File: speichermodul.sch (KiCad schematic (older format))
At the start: 64 parts, among them IC1 6116, P1 CONN_3X2, P2 CONN_01X01, P3 CONN_01X01, P4 CONN_01X01, P5 CONN_01X01, P6 CONN_01X01, P7 CONN_01X01, P8 CONN_02X10, P9 CONN_02X10, SW1 SW_PUSH, SW2 SW_PUSH, U1 7400, U2 74LS08, U3 74LS08, U4 74LS14, U5 74LS540, U6 74LS540

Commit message: Pcb layout kabelverlegt
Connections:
- net GND: no longer D10.1 (K), D11.1 (K), D12.1 (K), D13.1 (K), D14.1 (K), D15.1 (K), D16.1 (K), D17.1 (K), D18.1 (K), D3.1 (K), D4.1 (K), D5.1 (K), D6.1 (K), D7.1 (K), D8.1 (K), D9.1 (K)
- net VCC: now also D10.2 (A), D11.2 (A), D12.2 (A), D13.2 (A), D14.2 (A), D15.2 (A), D16.2 (A), D17.2 (A), D18.2 (A), D3.2 (A), D4.2 (A), D5.2 (A), D6.2 (A), D7.2 (A), D8.2 (A), D9.2 (A)
- net at R4.1: now also D10.1 (K); no longer D3.2 (A)
- net at R9.1: now also D9.1 (K); no longer D4.2 (A)
- net at R10.1: now also D8.1 (K); no longer D5.2 (A)
- net at R11.1: now also D7.1 (K); no longer D6.2 (A)
- net at R12.1: now also D6.1 (K); no longer D7.2 (A)
- net at R13.1: now also D5.1 (K); no longer D8.2 (A)
- net at R14.1: now also D4.1 (K); no longer D9.2 (A)
- net at R15.1: now also D3.1 (K); no longer D10.2 (A)
- net at R16.1: now also D18.1 (K); no longer D11.2 (A)
- net at R17.1: now also D17.1 (K); no longer D12.2 (A)
- net at R18.1: now also D16.1 (K); no longer D13.2 (A)
- net at R19.1: now also D15.1 (K); no longer D14.2 (A)
- net at R20.1: now also D14.1 (K); no longer D15.2 (A)
- net at R21.1: now also D13.1 (K); no longer D16.2 (A)
- net at R22.1: now also D12.1 (K); no longer D17.2 (A)
- net at R23.1: now also D11.1 (K); no longer D18.2 (A)
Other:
- moved on the sheet: D10, D11, D12, D13, D14, D15, D16, D17, D18, D3, D4, D5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

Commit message: PCB layout revolutioniert
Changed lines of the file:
@@
 Wire Wire Line
 	5800 1550 5800 1650
+Connection ~ 5800 1650
+Wire Wire Line
+	5800 1650 5800 1850
+Wire Wire Line
+	37600 -12100 37600 -21800
+Wire Wire Line
+	37600 -21800 42950 -21800
+Wire Wire Line
+	42950 -21800 42950 -11850
+Wire Wire Line
+	42950 -11850 54850 -11850
+Wire Wire Line
+	54850 -11850 54850 -1350
+Wire Wire Line
+	54850 -1350 47700 -1350
+Wire Wire Line
+	47700 -1350 47700 20550
+Wire Wire Line
+	47700 20550 41950 20550
+Wire Wire Line
+	41950 20550 41950 12350
+Wire Wire Line
+	41950 12350 38500 12350
+Wire Wire Line
+	38500 12350 38500 20300
+Wire Wire Line
+	38500 20300 32700 20300
+Wire Wire Line
+	32700 20300 32700 -3000
+Wire Wire Line
+	32700 -3000 22850 -3000
+Wire Wire Line
+	22850 -3000 22850 -6100
+Wire Wire Line
+	22850 -6100 18500 -6100
+Wire Wire Line
+	18500 -6100 18500 -8000
+Wire Wire Line
+	18500 -8000 22500 -8000
+Wire Wire Line
+	18500 -8000 18500 -9000
+Wire Wire Line
+	18500 -9000 22500 -9000
+Connection ~ 18500 -8000
+Wire Wire Line
+	14550 -12100 37600 -12100
+Wire Wire Line
+	14550 -12100 14550 -9800
+Wire Wire Line
+	18500 -9000 18500 -9800
+Connection ~ 18500 -9000
+Wire Wire Line
+	18500 -9800 14550 -9800
+Wire Wire Line
+	38600 -18050 39500 -18050
+Wire Wire Line
+	39500 -18050 39500 -17550
+Wire Wire Line
+	39500 -17550 38600 -17550
+Wire Wire Line
+	38600 -17550 38600 -18050
+Wire Wire Line
+	41150 -17500 42450 -17500
+Wire Wire Line
+	42450 -17500 42450 -18050
+Wire Wire Line
+	42450 -18050 41150 -18050
+Wire Wire Line
+	41150 -18050 41150 -17500
+Wire Wire Line
+	39950 -15200 40600 -15200
+Wire Wire Line
+	40600 -15200 40600 -16450
+Wire Wire Line
+	40600 -16450 39950 -16450
+Wire Wire Line
+	39950 -16450 39950 -15200
+Wire Wire Line
+	38400 -13700 38800 -13700
+Wire Wire Line
+	38800 -13700 38800 -13200
+Wire Wire Line
+	38800 -13200 39350 -13200
+Wire Wire Line
+	39350 -13200 39350 -12650
+Wire Wire Line
+	39350 -12650 41600 -12650
+Wire Wire Line
+	41600 -12650 41600 -13100
+Wire Wire Line
+	41600 -13100 42150 -13100
+Wire Wire Line
+	42150 -13100 42150 -13700
+Wire Wire Line
+	42150 -13700 42600 -13700
+Wire Wire Line
+	42600 -13700 42600 -14300
+Wire Wire Line
+	42600 -14300 41850 -14300
+Wire Wire Line
+	41850 -14300 41850 -13600
+Wire Wire Line
+	41850 -13600 41500 -13600
+Wire Wire Line
+	41500 -13600 41500 -13150
+Wire Wire Line
+	41500 -13150 39650 -13150
+Wire Wire Line
+	39650 -13150 39650 -13650
+Wire Wire Line
+	39650 -13650 39200 -13650
+Wire Wire Line
+	39200 -13650 39200 -14050
+Wire Wire Line
+	39200 -14050 38400 -14050
+Wire Wire Line
+	38400 -14050 38400 -13700
 Wire Bus Line
 	9550 3350 9550 3550
@@
 Wire Bus Line
 	10950 2750 10950 4850
-Connection ~ 5800 1650
-Wire Wire Line
-	5800 1650 5800 1850
 $EndSCHEMATC

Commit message: minimal änderungen
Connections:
- wire segments 262 -> 274
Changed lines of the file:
@@
 Wire Wire Line
 	38400 -14050 38400 -13700
+Wire Wire Line
+	55750 -26500 55750 -14450
+Wire Wire Line
+	55750 -14450 66900 -14450
+Wire Wire Line
+	71650 -25450 71650 -18950
+Wire Wire Line
+	71650 -18950 58050 -18950
+Wire Wire Line
+	66750 -25350 57150 -25350
+Wire Wire Line
+	57150 -25350 57150 -15850
+Wire Wire Line
+	57150 -15850 72550 -15850
+Wire Wire Line
+	60750 -21750 69950 -21750
+Wire Wire Line
+	69950 -21750 69950 -27500
+Wire Wire Line
+	69950 -27500 75100 -27500
+Wire Wire Line
+	75100 -27500 75100 -15100
+Wire Wire Line
+	75100 -15100 57050 -15100
 Wire Bus Line
 	9550 3350 9550 3550

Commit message: Nix
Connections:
- wire segments 274 -> 275
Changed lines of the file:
@@
 U 1 1 57D5C572
 P 9850 5250
-F 0 "P9" H 9850 5800 50  0000 C CNN
+F 0 "P9" H 9850 4650 50  0000 C CNN
 F 1 "CONN_02X10" V 9850 5250 50  0000 C CNN
 F 2 "Connect:IDC_Header_Straight_20pins" H 9850 4050 60  0001 C CNN
 F 3 "" H 9850 4050 60  0000 C CNN
 	1    9850 5250
-	-1   0    0    -1
+	-1   0    0    1
 $EndComp
 $Comp
@@
 F 3 "" H 9850 5800 60  0000 C CNN
 	1    9850 5800
-	-1   0    0    -1
+	1    0    0    -1
 $EndComp
-Text Notes 9650 4650 0    60   ~ 0
+Text Notes 10450 4800 0    60   ~ 0
 Datenbus
 Text Notes 10250 700  0    60   ~ 0
@@
 Wire Wire Line
 	10200 1850 10200 1750
-Wire Wire Line
-	10100 4800 10100 4650
-Wire Wire Line
-	10100 4650 9600 4650
-Wire Wire Line
-	10100 5800 10100 5700
 Wire Bus Line
 	10950 4850 10200 4850
@@
 	1300 4150 1300 4250
 Wire Wire Line
-	9600 5800 9850 5800
-Connection ~ 9850 5800
-Wire Wire Line
-	9850 5800 10100 5800
-Wire Wire Line
-	9600 4650 9600 4800
-Connection ~ 9600 5700
-Wire Wire Line
-	9600 5700 9600 5800
+	9600 4700 9850 4700
+Connection ~ 9850 4700
+Wire Wire Line
+	9850 4700 10100 4700
 Connection ~ 9600 4800
 Wire Wire Line
-	9600 4800 9600 4900
+	9600 4800 9600 4700
+Wire Wire Line
+	9600 5700 9600 5600
+Connection ~ 9600 5600
+Wire Wire Line
+	9600 5600 9600 5500
+Connection ~ 9600 5500
+Wire Wire Line
+	9600 5500 9600 5400
+Connection ~ 9600 5400
+Wire Wire Line
+	9600 5400 9600 5300
+Connection ~ 9600 5300
+Wire Wire Line
+	9600 5300 9600 5200
+Connection ~ 9600 5200
+Wire Wire Line
+	9600 5200 9600 5100
+Connection ~ 9600 5100
+Wire Wire Line
+	9600 5100 9600 5000
+Connection ~ 9600 5000
+Wire Wire Line
+	9600 5000 9600 4900
 Connection ~ 9600 4900
 Wire Wire Line
-	9600 4900 9600 5000
-Connection ~ 9600 5000
-Wire Wire Line
-	9600 5000 9600 5100
-Connection ~ 9600 5100
-Wire Wire Line
-	9600 5100 9600 5200
-Connection ~ 9600 5200
-Wire Wire Line
-	9600 5200 9600 5300
-Connection ~ 9600 5300
-Wire Wire Line
-	9600 5300 9600 5400
-Connection ~ 9600 5400
-Wire Wire Line
-	9600 5400 9600 5500
-Connection ~ 9600 5500
-Wire Wire Line
-	9600 5500 9600 5600
-Connection ~ 9600 5600
-Wire Wire Line
-	9600 5600 9600 5700
+	9600 4900 9600 4800
 Wire Wire Line
 	1300 2850 1300 2950
@@
 Wire Wire Line
 	75100 -15100 57050 -15100
+Wire Wire Line
+	10100 5800 10100 5700
+Wire Wire Line
+	10100 4700 10100 4800
+Wire Wire Line
+	10100 5800 9850 5800
+Wire Wire Line
+	9600 5800 9600 5700
 Wire Bus Line
 	9550 3350 9550 3550
@@
 	8100 1050 8100 1750
 Wire Bus Line
+	10950 2750 10950 4850
+Wire Bus Line
+	10200 4850 10200 6450
+Wire Bus Line
+	9550 2500 9550 3250
+Wire Bus Line
+	10100 850  10100 2500
+Wire Bus Line
+	9350 1200 9350 1750
+Wire Bus Line
 	7300 5750 7300 6450
-Wire Bus Line
-	9350 1200 9350 1750
-Wire Bus Line
-	10100 850  10100 2500
-Wire Bus Line
-	9550 2500 9550 3250
-Wire Bus Line
-	10200 4850 10200 6450
-Wire Bus Line
-	10950 2750 10950 4850
+Connection ~ 9600 5700
+Connection ~ 9850 5800
+Wire Wire Line
+	9850 5800 9600 5800
 $EndSCHEMATC

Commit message: mit Korrektur der Anordnung begonnen
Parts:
- removed RP3: R_PACK8BUSSED, Housings_SIP:SIP9_Housing_BigPads, symbol speichermodul-rescue:R_PACK8BUSSED-RESCUE-speichermodul
- SW1, SW2: footprint Buttons_Switches_ThroughHole:SW_PUSH_6mm_h5mm -> tg_foodprint:SW_PUSH_LCD_E3_SAxxxx_tg
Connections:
- wire segments 275 -> 280
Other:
- moved on the sheet: RP2
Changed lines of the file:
@@
 F 0 "SW2" H 1150 4960 50  0000 C CNN
 F 1 "SW_PUSH" H 1000 4770 50  0000 C CNN
-F 2 "Buttons_Switches_ThroughHole:SW_PUSH_6mm_h5mm" H 1000 4850 60  0001 C CNN
+F 2 "tg_foodprint:SW_PUSH_LCD_E3_SAxxxx_tg" H 1000 4850 60  0001 C CNN
 F 3 "~" H 1000 4850 60  0000 C CNN
 	1    1000 4850
@@
 F 0 "SW1" H 1150 2760 50  0000 C CNN
 F 1 "SW_PUSH" H 1000 2570 50  0000 C CNN
-F 2 "Buttons_Switches_ThroughHole:SW_PUSH_6mm_h5mm" H 1000 2650 60  0001 C CNN
+F 2 "tg_foodprint:SW_PUSH_LCD_E3_SAxxxx_tg" H 1000 2650 60  0001 C CNN
 F 3 "~" H 1000 2650 60  0000 C CNN
 	1    1000 2650
@@
 L speichermodul-rescue:R_PACK8BUSSED-RESCUE-speichermodul RP2
 U 1 1 57D77728
-P 9050 1250
-F 0 "RP2" H 9050 1550 50  0000 C CNN
-F 1 "R_PACK8BUSSED" H 9050 950 50  0000 C CNN
-F 2 "Housings_SIP:SIP9_Housing_BigPads" H 9050 1300 60  0001 C CNN
-F 3 "~" H 9050 1300 60  0000 C CNN
-	1    9050 1250
+P 9000 1250
+F 0 "RP2" H 9000 1550 50  0000 C CNN
+F 1 "R_PACK8BUSSED" H 9000 950 50  0000 C CNN
+F 2 "Housings_SIP:SIP9_Housing_BigPads" H 9000 1300 60  0001 C CNN
+F 3 "~" H 9000 1300 60  0000 C CNN
+	1    9000 1250
 	-1   0    0    -1
 $EndComp
@@
 Wire Wire Line
 	9350 1050 9350 1000
-$Comp
-L speichermodul-rescue:R_PACK8BUSSED-RESCUE-speichermodul RP3
-U 1 1 57D77ABD
-P 7000 5800
-F 0 "RP3" H 7000 6100 50  0000 C CNN
-F 1 "R_PACK8BUSSED" H 7000 5500 50  0000 C CNN
-F 2 "Housings_SIP:SIP9_Housing_BigPads" H 7000 5850 60  0000 C CNN
-F 3 "~" H 7000 5850 60  0000 C CNN
-	1    7000 5800
-	-1   0    0    -1
-$EndComp
-$Comp
-L speichermodul-rescue:VCC-RESCUE-speichermodul #PWR025
-U 1 1 57D77ACC
-P 7300 5550
-F 0 "#PWR025" H 7300 5400 50  0001 C CNN
-F 1 "VCC" H 7300 5700 50  0000 C CNN
-F 2 "" H 7300 5550 60  0000 C CNN
-F 3 "" H 7300 5550 60  0000 C CNN
-	1    7300 5550
-	1    0    0    -1
-$EndComp
-Wire Wire Line
-	7300 5600 7300 5550
 Wire Bus Line
 	4450 6450 10200 6450
 Entry Wire Line
-	7200 5650 7300 5750
-Entry Wire Line
-	7200 5700 7300 5800
-Entry Wire Line
-	7200 5750 7300 5850
-Entry Wire Line
-	7200 5800 7300 5900
-Entry Wire Line
-	7200 5850 7300 5950
-Entry Wire Line
-	7200 5900 7300 6000
-Entry Wire Line
-	7200 5950 7300 6050
-Entry Wire Line
-	7200 6000 7300 6100
-Wire Wire Line
-	7300 5600 7200 5600
-Text Label 7200 5650 0    60   ~ 0
-D0
-Text Label 7200 5700 0    60   ~ 0
-D1
-Text Label 7200 5750 0    60   ~ 0
-D2
-Text Label 7200 5800 0    60   ~ 0
-D3
-Text Label 7200 5850 0    60   ~ 0
-D4
-Text Label 7200 5900 0    60   ~ 0
-D5
-Text Label 7200 5950 0    60   ~ 0
-D6
-Text Label 7200 6000 0    60   ~ 0
-D7
-Entry Wire Line
 	9250 1100 9350 1200
 Entry Wire Line
@@
 Entry Wire Line
 	9250 1450 9350 1550
-Wire Wire Line
-	9250 1050 9350 1050
 Text Label 9250 1100 0    60   ~ 0
 A0
@@
 Wire Wire Line
 	1300 4150 1300 4250
-Wire Wire Line
-	9600 4700 9850 4700
-Connection ~ 9850 4700
-Wire Wire Line
-	9850 4700 10100 4700
 Connection ~ 9600 4800
 Wire Wire Line
@@
 Wire Wire Line
 	9600 5800 9600 5700
+Connection ~ 9600 5700
+Connection ~ 9850 5800
+Wire Wire Line
+	9850 5800 9600 5800
+Wire Wire Line
+	9600 4700 10100 4700
+Wire Wire Line
+	9200 1050 9350 1050
+Wire Wire Line
+	9250 1100 9200 1100
+Wire Wire Line
+	9200 1150 9250 1150
+Wire Wire Line
+	9250 1200 9200 1200
+Wire Wire Line
+	9200 1250 9250 1250
+Wire Wire Line
+	9250 1300 9200 1300
+Wire Wire Line
+	9200 1350 9250 1350
+Wire Wire Line
+	9250 1400 9200 1400
+Wire Wire Line
+	9200 1450 9250 1450
 Wire Bus Line
 	9550 3350 9550 3550
@@
 Wire Bus Line
 	9350 1200 9350 1750
-Wire Bus Line
-	7300 5750 7300 6450
-Connection ~ 9600 5700
-Connection ~ 9850 5800
-Wire Wire Line
-	9850 5800 9600 5800
 $EndSCHEMATC

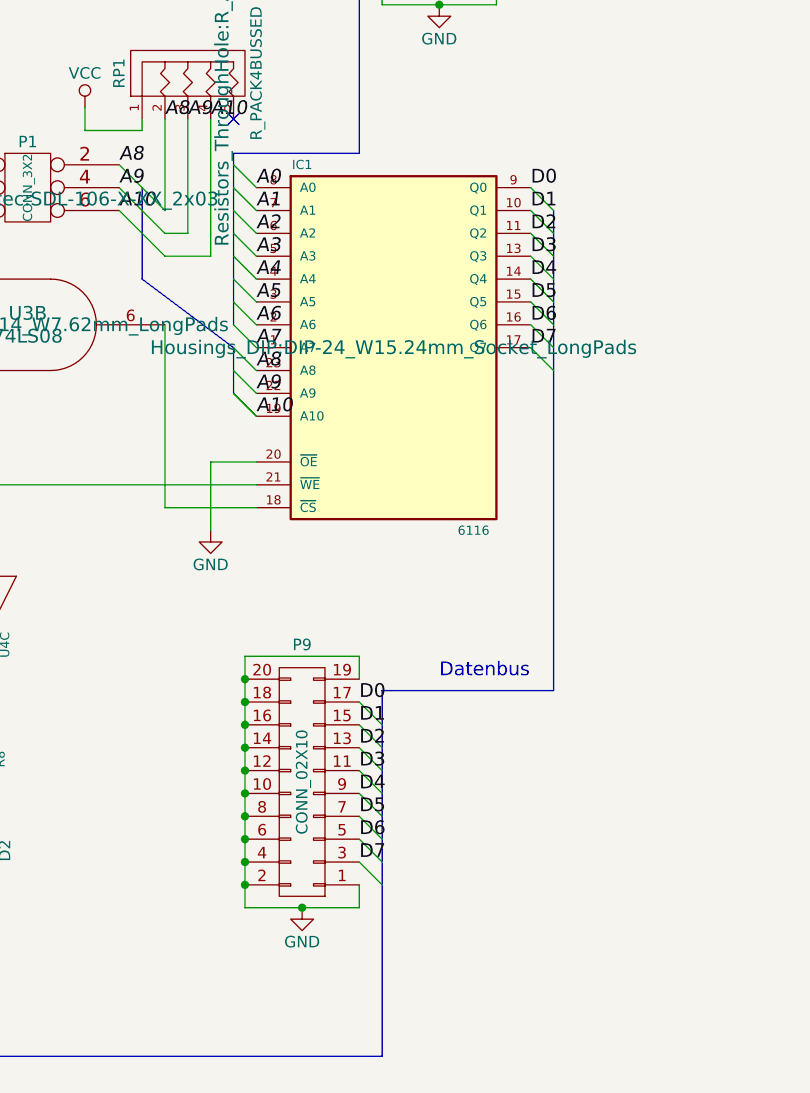
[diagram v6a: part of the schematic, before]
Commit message: busses new arranged
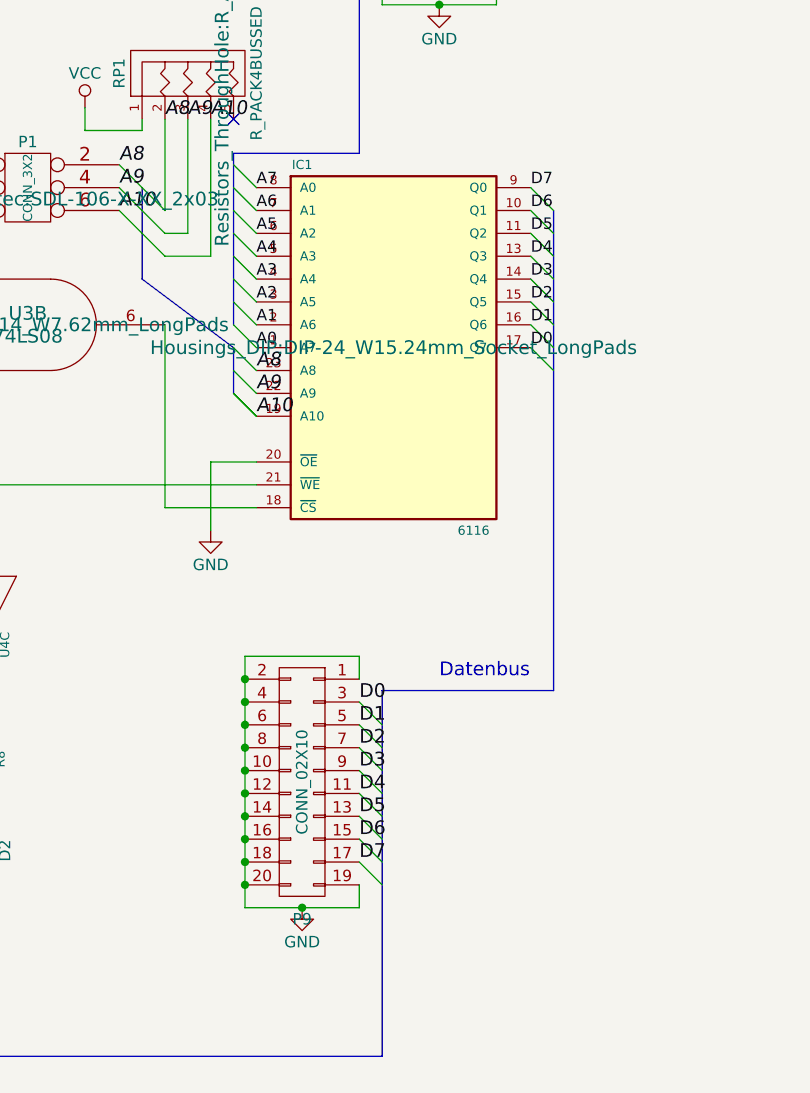
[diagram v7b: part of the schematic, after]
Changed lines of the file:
@@
 F 3 "" H 9850 4050 60  0000 C CNN
 	1    9850 5250
-	-1   0    0    1
+	-1   0    0    -1
 $EndComp
 $Comp
@@
 Entry Wire Line
 	10850 2650 10950 2750
-Text Label 10850 2650 0    60   ~ 0
-D0
-Text Label 10850 2750 0    60   ~ 0
-D1
-Text Label 10850 2850 0    60   ~ 0
-D2
-Text Label 10850 2950 0    60   ~ 0
-D3
-Text Label 10850 3050 0    60   ~ 0
-D4
-Text Label 10850 3150 0    60   ~ 0
-D5
-Text Label 10850 3250 0    60   ~ 0
-D6
-Text Label 10850 3350 0    60   ~ 0
-D7
 Entry Wire Line
 	10850 2750 10950 2850
@@
 Text Label 10200 1650 0    60   Italic 0
 A7
-Text Label 9650 2650 0    60   Italic 0
-A0
-Text Label 9650 2750 0    60   Italic 0
-A1
-Text Label 9650 2850 0    60   Italic 0
-A2
-Text Label 9650 2950 0    60   Italic 0
-A3
-Text Label 9650 3050 0    60   Italic 0
-A4
-Text Label 9650 3150 0    60   Italic 0
-A5
-Text Label 9650 3250 0    60   Italic 0
-A6
-Text Label 9650 3350 0    60   Italic 0
-A7
-Entry Wire Line
-	9550 2550 9650 2650
-Entry Wire Line
-	9550 2650 9650 2750
-Entry Wire Line
-	9550 2750 9650 2850
-Entry Wire Line
-	9550 2850 9650 2950
-Entry Wire Line
-	9550 2950 9650 3050
-Entry Wire Line
-	9550 3050 9650 3150
-Entry Wire Line
-	9550 3150 9650 3250
-Entry Wire Line
-	9550 3250 9650 3350
 Connection ~ 1150 4150
 Wire Wire Line
@@
 Wire Wire Line
 	1300 4150 1300 4250
-Connection ~ 9600 4800
-Wire Wire Line
-	9600 4800 9600 4700
-Wire Wire Line
-	9600 5700 9600 5600
-Connection ~ 9600 5600
-Wire Wire Line
-	9600 5600 9600 5500
-Connection ~ 9600 5500
-Wire Wire Line
-	9600 5500 9600 5400
-Connection ~ 9600 5400
-Wire Wire Line
-	9600 5400 9600 5300
-Connection ~ 9600 5300
-Wire Wire Line
-	9600 5300 9600 5200
-Connection ~ 9600 5200
-Wire Wire Line
-	9600 5200 9600 5100
-Connection ~ 9600 5100
-Wire Wire Line
-	9600 5100 9600 5000
-Connection ~ 9600 5000
-Wire Wire Line
-	9600 5000 9600 4900
-Connection ~ 9600 4900
-Wire Wire Line
-	9600 4900 9600 4800
 Wire Wire Line
 	1300 2850 1300 2950
@@
 Wire Wire Line
 	10100 5800 9850 5800
-Wire Wire Line
-	9600 5800 9600 5700
+Connection ~ 9850 5800
+Wire Wire Line
+	9850 5800 9600 5800
+Wire Wire Line
+	9600 4700 10100 4700
+Wire Wire Line
+	9200 1050 9350 1050
+Wire Wire Line
+	9250 1100 9200 1100
+Wire Wire Line
+	9200 1150 9250 1150
+Wire Wire Line
+	9250 1200 9200 1200
+Wire Wire Line
+	9200 1250 9250 1250
+Wire Wire Line
+	9250 1300 9200 1300
+Wire Wire Line
+	9200 1350 9250 1350
+Wire Wire Line
+	9250 1400 9200 1400
+Wire Wire Line
+	9200 1450 9250 1450
+Entry Wire Line
+	9550 3250 9650 3350
+Entry Wire Line
+	9550 3150 9650 3250
+Entry Wire Line
+	9550 3050 9650 3150
+Entry Wire Line
+	9550 2950 9650 3050
+Entry Wire Line
+	9550 2850 9650 2950
+Entry Wire Line
+	9550 2750 9650 2850
+Entry Wire Line
+	9550 2650 9650 2750
+Entry Wire Line
+	9550 2550 9650 2650
+Text Label 9650 3350 0    50   ~ 0
+A0
+Text Label 9650 3250 0    50   ~ 0
+A1
+Text Label 9650 3150 0    50   ~ 0
+A2
+Text Label 9650 3050 0    50   ~ 0
+A3
+Text Label 9650 2950 0    50   ~ 0
+A4
+Text Label 9650 2850 0    50   ~ 0
+A5
+Text Label 9650 2750 0    50   ~ 0
+A6
+Text Label 9650 2650 0    50   ~ 0
+A7
+Wire Wire Line
+	9600 4700 9600 4800
+Wire Wire Line
+	9600 5700 9600 5800
+Wire Wire Line
+	9600 4800 9600 4900
+Connection ~ 9600 4800
 Connection ~ 9600 5700
-Connection ~ 9850 5800
-Wire Wire Line
-	9850 5800 9600 5800
-Wire Wire Line
-	9600 4700 10100 4700
-Wire Wire Line
-	9200 1050 9350 1050
-Wire Wire Line
-	9250 1100 9200 1100
-Wire Wire Line
-	9200 1150 9250 1150
-Wire Wire Line
-	9250 1200 9200 1200
-Wire Wire Line
-	9200 1250 9250 1250
-Wire Wire Line
-	9250 1300 9200 1300
-Wire Wire Line
-	9200 1350 9250 1350
-Wire Wire Line
-	9250 1400 9200 1400
-Wire Wire Line
-	9200 1450 9250 1450
+Connection ~ 9600 4900
+Wire Wire Line
+	9600 4900 9600 5000
+Connection ~ 9600 5000
+Wire Wire Line
+	9600 5000 9600 5100
+Connection ~ 9600 5100
+Wire Wire Line
+	9600 5100 9600 5200
+Connection ~ 9600 5200
+Wire Wire Line
+	9600 5200 9600 5300
+Connection ~ 9600 5300
+Wire Wire Line
+	9600 5300 9600 5400
+Connection ~ 9600 5400
+Wire Wire Line
+	9600 5400 9600 5500
+Connection ~ 9600 5500
+Wire Wire Line
+	9600 5500 9600 5600
+Connection ~ 9600 5600
+Wire Wire Line
+	9600 5600 9600 5700
 Wire Bus Line
 	9550 3350 9550 3550
@@
 	8100 1050 8100 1750
 Wire Bus Line
+	9550 2500 9550 3250
+Wire Bus Line
 	10950 2750 10950 4850
 Wire Bus Line
 	10200 4850 10200 6450
 Wire Bus Line
-	9550 2500 9550 3250
-Wire Bus Line
 	10100 850  10100 2500
 Wire Bus Line
 	9350 1200 9350 1750
+Text Label 10850 2650 0    50   ~ 0
+D7
+Text Label 10850 2750 0    50   ~ 0
+D6
+Text Label 10850 2850 0    50   ~ 0
+D5
+Text Label 10850 2950 0    50   ~ 0
+D4
+Text Label 10850 3050 0    50   ~ 0
+D3
+Text Label 10850 3150 0    50   ~ 0
+D2
+Text Label 10850 3250 0    50   ~ 0
+D1
+Text Label 10850 3350 0    50   ~ 0
+D0
 $EndSCHEMATC

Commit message: Powerpins neu gemacht
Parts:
- removed C1: 0, Capacitors_ThroughHole:C_Disc_D10.0mm_W2.5mm_P5.00mm, symbol speichermodul-rescue:C-RESCUE-speichermodul
- removed P2, P3, P4, P5, P6, P7: CONN_01X01, Pin_Headers:Pin_Header_Straight_1x01_Pitch1.27mm, symbol speichermodul-rescue:CONN_01X01-RESCUE-speichermodul
- added C1, C2, C3, C4, C5, C6, C7: 100n, Capacitors_ThroughHole:C_Disc_D10.0mm_W2.5mm_P5.00mm, symbol bonsai:C
- added D36: D, Diodes_ThroughHole:D_DO-41_SOD81_P10.16mm_Horizontal, symbol bonsai:D
- added J1, J2, J3: 2PinTerminalBlocktg, 2PinTerminalBlocktg, symbol 2PinTerminalBlocktg:2PinTerminalBlocktg
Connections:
- net labels added: AUTO, EN, RD, WR
- wire segments 280 -> 317
